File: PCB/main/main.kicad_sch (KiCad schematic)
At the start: 10 parts, among them J1 Conn_01x06_Pin, J2 Conn_01x05_Pin, J3 Conn_01x05_Pin, J4 Conn_01x06_Pin, J5 Conn_01x06_Pin, U1 ATtiny1614-SS, U2 TB6612FNG

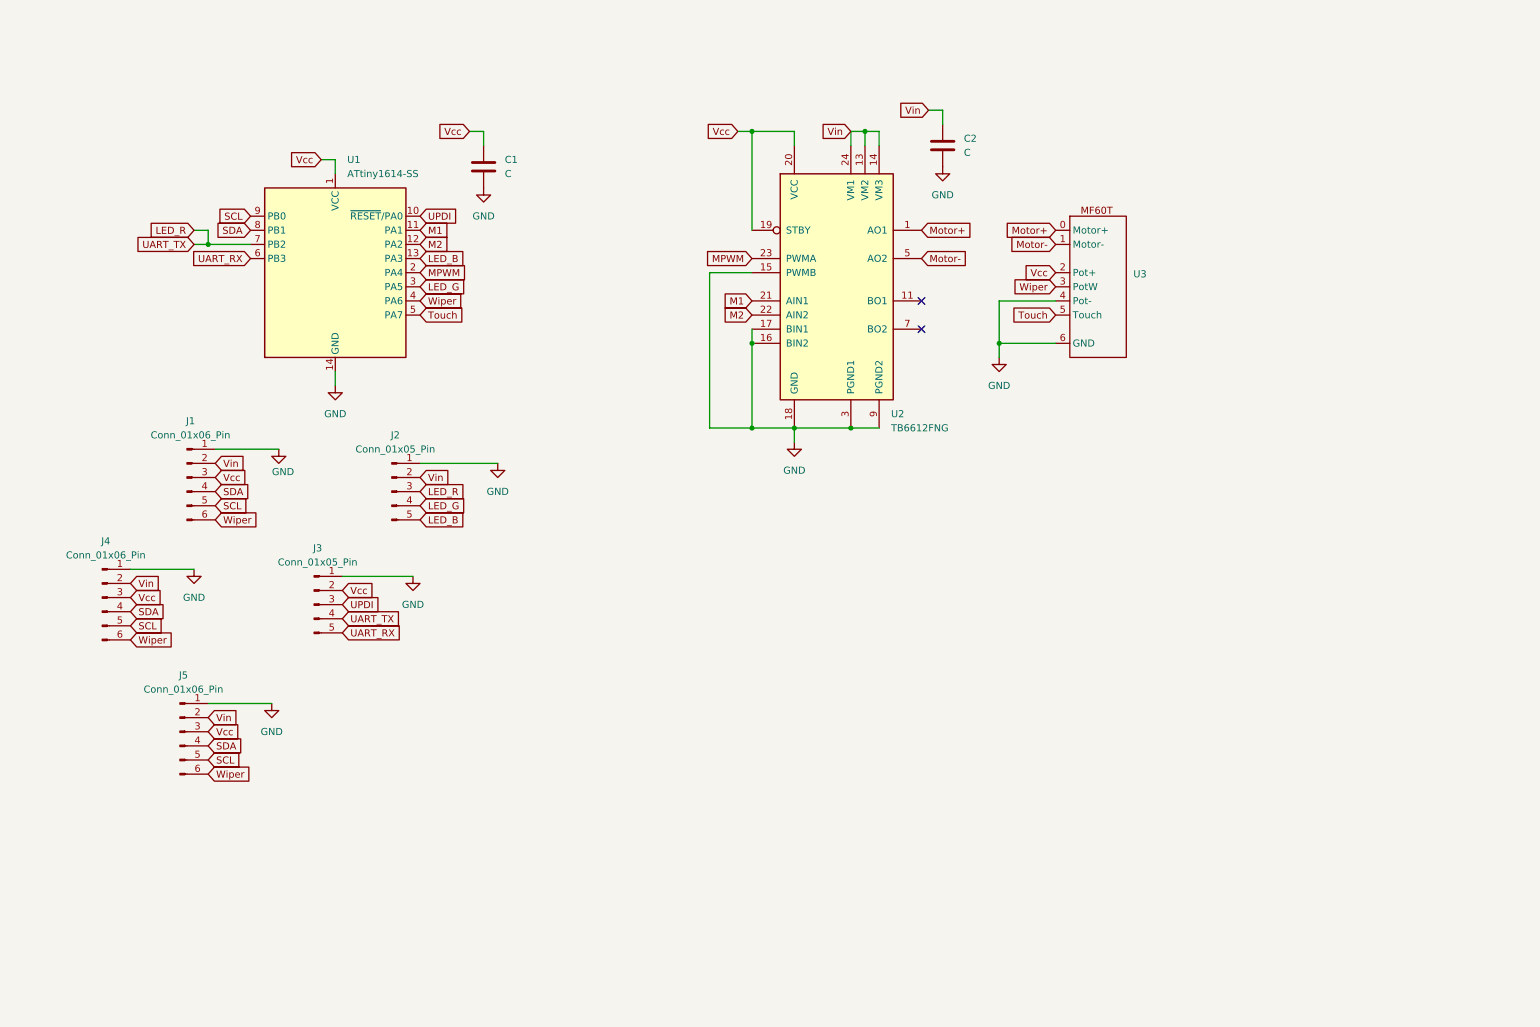
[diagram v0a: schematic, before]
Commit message: Initial commit on rp2040 version
Switching to the cheaper, more capable RP2040 with an additional change from the I2C protocol to a daisy-chained serial protocol.
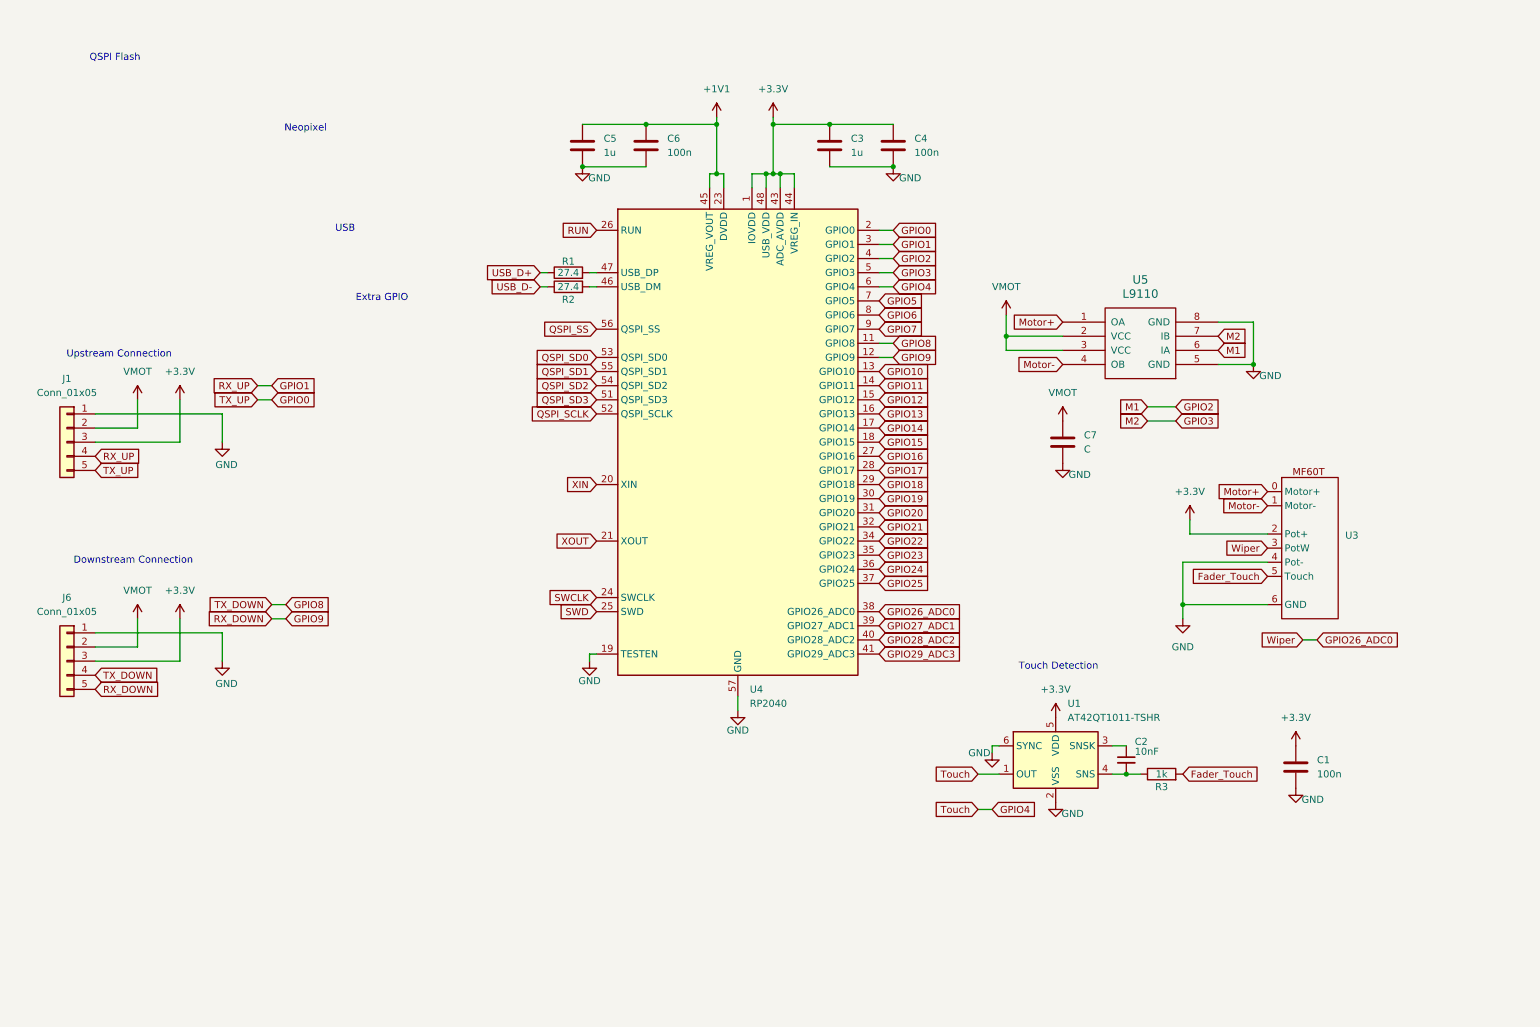
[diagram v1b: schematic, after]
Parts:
- removed C2: C, Capacitor_SMD:C_1206_3216Metric_Pad1.33x1.80mm_HandSolder, symbol Device:C
- removed J1, J4, J5: Conn_01x06_Pin, Connector_PinHeader_2.54mm:PinHeader_1x06_P2.54mm_Vertical, symbol Connector:Conn_01x06_Pin
- removed J2, J3: Conn_01x05_Pin, Connector_PinHeader_2.54mm:PinHeader_1x05_P2.54mm_Vertical, symbol Connector:Conn_01x05_Pin
- removed U1: ATtiny1614-SS, Package_SO:SOIC-14_3.9x8.7mm_P1.27mm, symbol MCU_Microchip_ATtiny:ATtiny1614-SS
- removed U2: TB6612FNG, Package_SO:SSOP-24_5.3x8.2mm_P0.65mm, symbol Driver_Motor:TB6612FNG
- added C2: 10nF, symbol Device:C_Small
- added C3, C5: 1u, symbol Device:C
- added C4, C6: 100n, symbol Device:C
- added C7: C, Capacitor_SMD:C_1206_3216Metric_Pad1.33x1.80mm_HandSolder, symbol Device:C
- added J1, J6: Conn_01x05, Connector_JST:JST_XH_B5B-XH-AM_1x05_P2.50mm_Vertical, symbol Connector_Generic:Conn_01x05
- added R1, R2: 27.4, symbol Device:R
- added R3: 1k, symbol Device:R
- added U1: AT42QT1011-TSHR, Package_TO_SOT_SMD:SOT-23-6, symbol Sensor_Touch:AT42QT1011-TSHR
- added U4: RP2040, Package_DFN_QFN:QFN-56-1EP_7x7mm_P0.4mm_EP3.2x3.2mm, symbol MCU_RaspberryPi:RP2040
- added U5: L9110, symbol L9110:L9110
- C1: value C -> 100n; footprint Capacitor_SMD:C_1206_3216Metric_Pad1.33x1.80mm_HandSolder -> (none)
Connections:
- net GND: now also C3.2, C4.2, C5.2, C6.2, C7.2, J1.1 (Pin_1), J6.1 (Pin_1), U1.2 (VSS), U1.6 (SYNC), U4.19 (TESTEN), U4.57 (GND), U5.5 (GND), U5.8 (GND)
- net Motor+: now also U5.1 (OA)
- net Motor-: now also U5.4 (OB)
- net Touch renamed Fader_Touch
- net Fader_Touch: now also R3.2
- net Vcc renamed +3.3V
- net +3.3V: now also C3.1, C4.1, J1.3 (Pin_3), J6.3 (Pin_3), U1.5 (VDD), U4.1 (IOVDD), U4.10 (IOVDD), U4.22 (IOVDD), U4.33 (IOVDD), U4.42 (IOVDD), U4.43 (ADC_AVDD), U4.44 (VREG_IN), U4.48 (USB_VDD), U4.49 (IOVDD)
- net Wiper renamed GPIO26_ADC0
- net GPIO26_ADC0: now also U4.38 (GPIO26_ADC0)
- new net: C2.2, R3.1, U1.4 (SNS)
- new net: R2.2, U4.46 (USB_DM)
- new net: C2.1, U1.3 (SNSK)
- new net: R1.2, U4.47 (USB_DP)
- new net +1V1: C5.1, C6.1, U4.23 (DVDD), U4.45 (VREG_VOUT), U4.50 (DVDD)
- new net GPIO0: J1.5 (Pin_5), U4.2 (GPIO0)
- new net GPIO1: J1.4 (Pin_4), U4.3 (GPIO1)
- new net GPIO10: U4.13 (GPIO10)
- new net GPIO11: U4.14 (GPIO11)
- new net GPIO12: U4.15 (GPIO12)
- new net GPIO13: U4.16 (GPIO13)
- new net GPIO14: U4.17 (GPIO14)
- new net GPIO15: U4.18 (GPIO15)
- new net GPIO16: U4.27 (GPIO16)
- new net GPIO17: U4.28 (GPIO17)
- new net GPIO18: U4.29 (GPIO18)
- new net GPIO19: U4.30 (GPIO19)
- new net GPIO2: U4.4 (GPIO2), U5.6 (IA)
- new net GPIO20: U4.31 (GPIO20)
- new net GPIO21: U4.32 (GPIO21)
- new net GPIO22: U4.34 (GPIO22)
- new net GPIO23: U4.35 (GPIO23)
- new net GPIO24: U4.36 (GPIO24)
- new net GPIO25: U4.37 (GPIO25)
- new net GPIO27_ADC1: U4.39 (GPIO27_ADC1)
- new net GPIO28_ADC2: U4.40 (GPIO28_ADC2)
- new net GPIO29_ADC3: U4.41 (GPIO29_ADC3)
- new net GPIO3: U4.5 (GPIO3), U5.7 (IB)
- new net GPIO4: U1.1 (OUT), U4.6 (GPIO4)
- new net GPIO5: U4.7 (GPIO5)
- new net GPIO6: U4.8 (GPIO6)
- new net GPIO7: U4.9 (GPIO7)
- new net GPIO8: J6.4 (Pin_4), U4.11 (GPIO8)
- new net GPIO9: J6.5 (Pin_5), U4.12 (GPIO9)
- new net QSPI_SCLK: U4.52 (QSPI_SCLK)
- new net QSPI_SD0: U4.53 (QSPI_SD0)
- new net QSPI_SD1: U4.55 (QSPI_SD1)
- new net QSPI_SD2: U4.54 (QSPI_SD2)
- new net QSPI_SD3: U4.51 (QSPI_SD3)
- new net QSPI_SS: U4.56 (QSPI_SS)
- new net RUN: U4.26 (RUN)
- new net SWCLK: U4.24 (SWCLK)
- new net SWD: U4.25 (SWD)
- new net USB_D+: R1.1
- new net USB_D-: R2.1
- new net VMOT: C7.1, J1.2 (Pin_2), J6.2 (Pin_2), U5.2 (VCC), U5.3 (VCC)
- new net XIN: U4.20 (XIN)
- new net XOUT: U4.21 (XOUT)
- no-connect marks 2 -> 0
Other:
- note added: "Downstream Connection"
- note added: "Extra GPIO"
- note added: "Neopixel"
- note added: "QSPI Flash"
- note added: "Touch Detection"
- note added: "USB"
- note added: "Upstream Connection"
- moved on the sheet: U3

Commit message: Progress on new PCB schematic
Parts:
- added C10, C11: 15p, symbol Device:C
- added C8: 4.7nF, symbol Device:C_Small
- added C9: 100n, symbol Device:C
- added D1, D2: D_Schottky, symbol Device:D_Schottky
- added D3: APA-106-F5, LED_THT:LED_D5.0mm-4_RGB, symbol LED:APA-106-F5
- added J2: USB_C_Receptacle_USB2.0_16P, Connector_USB:USB_C_Receptacle_GCT_USB4110, symbol Connector:USB_C_Receptacle_USB2.0_16P
- added J3: Conn_01x03_Pin, symbol Connector:Conn_01x03_Pin
- added R10, R8: 10k, symbol Device:R
- added R11: 15k, symbol Device:R
- added R4: 1M, symbol Device:R
- added R5, R6: 5.1k, symbol Device:R
- added R7, R9: 1k, symbol Device:R
- added SW1: Reset, symbol Switch:SW_Push
- added SW2: Boot, symbol Switch:SW_Push
- added TP1: 10, symbol Connector:TestPoint
- added TP10: 19, symbol Connector:TestPoint
- added TP11: 20, symbol Connector:TestPoint
- added TP12: 21, symbol Connector:TestPoint
- added TP13: 22, symbol Connector:TestPoint
- added TP14: 23, symbol Connector:TestPoint
- added TP15: 24, symbol Connector:TestPoint
- added TP16: 25, symbol Connector:TestPoint
- added TP2: 11, symbol Connector:TestPoint
- added TP3: 12, symbol Connector:TestPoint
- added TP4: 13, symbol Connector:TestPoint
- added TP5: 14, symbol Connector:TestPoint
- added TP6: 15, symbol Connector:TestPoint
- added TP7: 16, symbol Connector:TestPoint
- added TP8: 17, symbol Connector:TestPoint
- added TP9: 18, symbol Connector:TestPoint
- added U2: AMS1117-3.3, Package_TO_SOT_SMD:SOT-223-3_TabPin2, symbol Regulator_Linear:AMS1117-3.3
- added U6: MX25L3233FM, Package_SO:SOIC-16W_7.5x10.3mm_P1.27mm, symbol Memory_Flash:MX25L3233FM
- added Y1: ABM8G-12.000MHZ-D2Y-T, CRYSTAL_ABM8G_ABR, symbol 2026-04-12_02-59-10:ABM8G-12.000MHZ-D2Y-T
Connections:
- net +3.3V: now also C9.1, R8.2, U2.2 (VO), U6.2 (VCC); no longer J1.3 (Pin_3), J6.3 (Pin_3)
- net GND: now also C10.1, C11.1, C8.2, C9.2, D3.2 (GND), J2.A1 (GND), J2.A12 (GND), J2.B1 (GND), J2.B12 (GND), J3.3 (Pin_3), R11.1, R4.2, R5.2, R6.1, SW1.1, SW2.1, U2.1 (GND), U6.10 (GND), Y1.2, Y1.4
- net GPIO10: now also TP1.1
- net GPIO11: now also TP2.1
- net GPIO12: now also TP3.1
- net GPIO13: now also TP4.1
- net GPIO14: now also TP5.1
- net GPIO15: now also TP6.1
- net GPIO16: now also TP7.1
- net GPIO17: now also TP8.1
- net GPIO18: now also TP9.1
- net GPIO19: now also TP10.1
- net GPIO20: now also TP11.1
- net GPIO21: now also TP12.1
- net GPIO22: now also TP13.1
- net GPIO23: now also TP14.1
- net GPIO24: now also TP15.1
- net GPIO25: now also TP16.1
- net GPIO5: now also D3.4 (DI)
- net GPIO6: now also R10.1, R11.2
- net QSPI_SCLK: now also U6.16 (SCLK)
- net QSPI_SD0: now also U6.15 (SI/SIO0)
- net QSPI_SD1: now also U6.8 (SO/SIO1)
- net QSPI_SD2: now also U6.9 (~{WP}/SIO2)
- net QSPI_SD3: now also U6.1 (~{HOLD}/SIO3)
- net QSPI_SS: now also R7.1, R8.1, U6.7 (~{CS})
- net SWCLK: now also J3.1 (Pin_1)
- net SWD: now also J3.2 (Pin_2)
- net USB_D+: now also J2.A6 (D+), J2.B6 (D+)
- net USB_D-: now also J2.A7 (D-), J2.B7 (D-)
- net VMOT: now also D2.1 (K)
- net XIN: now also C10.2, Y1.1
- net XOUT: now also R9.1
- new net: C8.1, J2.S1 (SHIELD), R4.1
- new net: C11.2, R9.2, Y1.3
- new net: J2.A5 (CC1), R5.1
- new net: J2.B5 (CC2), R6.2
- new net +5V: D1.1 (K), D3.3 (VDD), J1.3 (Pin_3), J6.3 (Pin_3), U2.3 (VI)
- new net BOOT_BTN: R7.2, SW2.2
- new net RESET_BTN: SW1.2
- new net RGB_DOUT: D3.1 (DO)
- new net USB_VBUS: D1.2 (A), D2.2 (A), J2.A4 (VBUS), J2.A9 (VBUS), J2.B4 (VBUS), J2.B9 (VBUS), R10.2
- no-connect marks 0 -> 2
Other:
- note added: "Voltage regulator (optional through hole for master device) or maybe solder jumper"
- moved on the sheet: C1, C2, C3, C4, C5, C6, C7, J1, J6, R1, R2, R3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

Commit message: Progress on schematic
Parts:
- added C12, C13: 10u, symbol Device:C
- added R12: 470, symbol Device:R
- added TP17: 7, symbol Connector:TestPoint
- TP15: value 24 -> 25
- TP16: value 25 -> 6
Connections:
- net RESET_BTN is gone; now on net RUN: SW1.2
- net +3.3V: now also C13.1
- net +5V: now also C12.1
- net GND: now also J3.2 (Pin_2), C12.2, C13.2; no longer J3.3 (Pin_3)
- net GPIO24: now also R10.1, R11.2; no longer TP15.1
- net GPIO25: now also TP15.1; no longer TP16.1
- net GPIO5: now also R12.1; no longer D3.4 (DI)
- net GPIO6: now also TP16.1; no longer R10.1, R11.2
- net GPIO7: now also TP17.1
- net SWCLK: now also J3.3 (Pin_3); no longer J3.1 (Pin_1)
- net SWD: now also J3.1 (Pin_1); no longer J3.2 (Pin_2)
- new net: D3.4 (DI), R12.2
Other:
- moved on the sheet: J3, TP1, TP10, TP11, TP12, TP13, TP14, TP15, TP2, TP3, TP4, TP5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

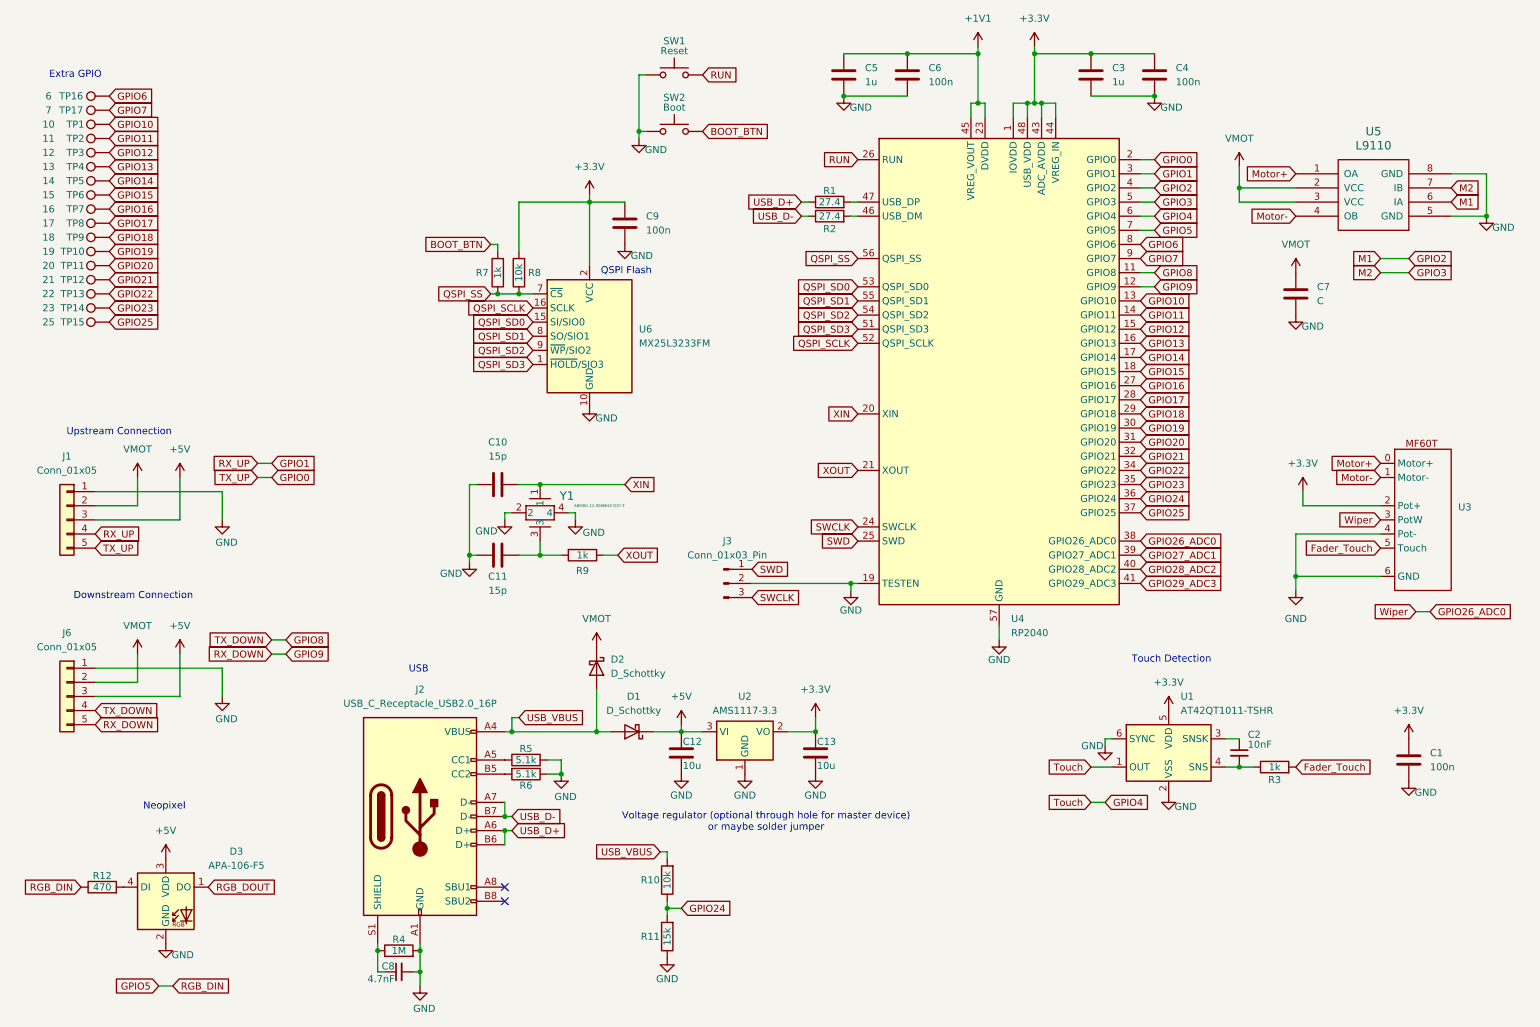
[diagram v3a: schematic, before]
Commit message: Schematic Updates
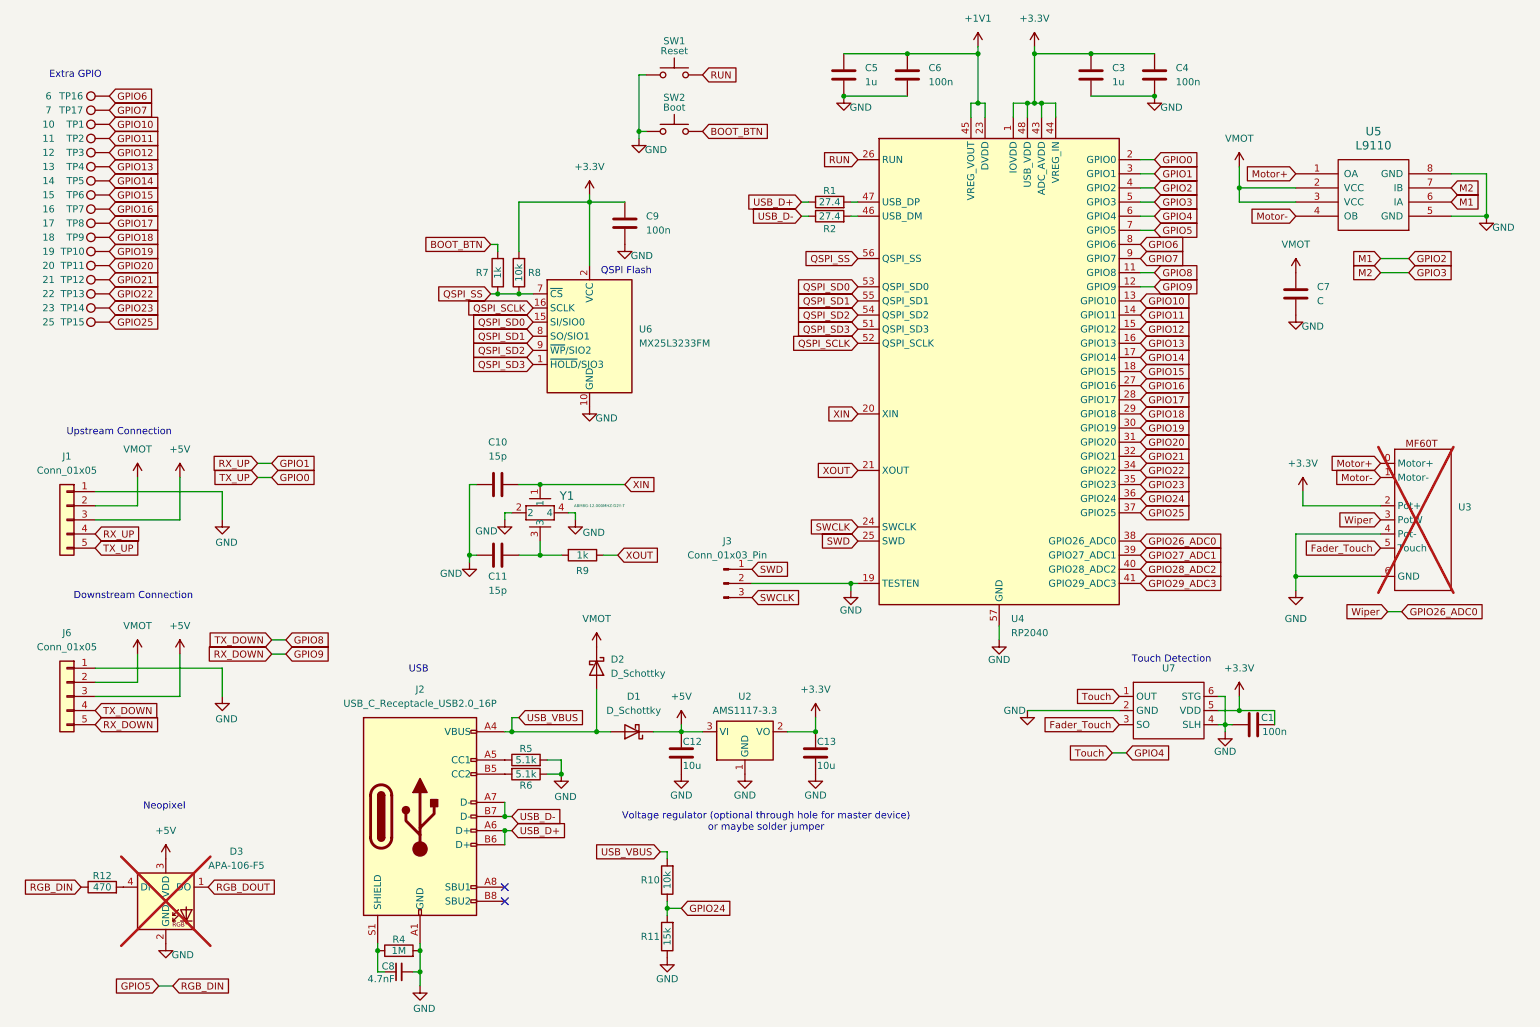
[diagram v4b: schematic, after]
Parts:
- removed C2: 10nF, symbol Device:C_Small
- removed R3: 1k, symbol Device:R
- removed U1: AT42QT1011-TSHR, Package_TO_SOT_SMD:SOT-23-6, symbol Sensor_Touch:AT42QT1011-TSHR
- added U7: (no value), EasyEDA_Lib:SOT-23-6_L2.9-W1.6-P0.95-LS2.9-BL, symbol EasyEDA_Lib:TTP223-BA6-TD
- D3: now not fitted; now left out of the parts list
- U3: value ~ -> (none); now not fitted; now left out of the parts list
- U5: LCSC (none) -> C513306
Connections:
- net +3.3V: now also U7.5 (VDD)
- net Fader_Touch: now also U7.3 (SO)
- net GND: now also U7.2 (GND), U7.4 (SLH), U7.6 (STG)
- net GPIO4: now also U7.1 (OUT)
